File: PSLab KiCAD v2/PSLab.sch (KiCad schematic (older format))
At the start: 73 parts, among them CON1 USB-MINI-B, P10 Analog, P12 5V, P13 MCLR, P2 PROG, P3 DIO, P4 V+/V-, P5 sen-cap, P6 I2C, P7 NRF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

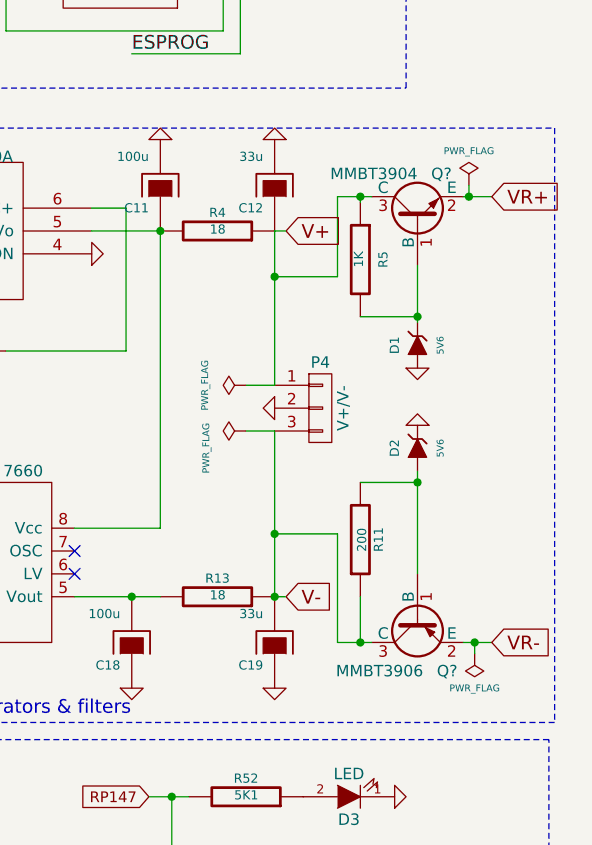
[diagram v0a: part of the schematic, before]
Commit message: Edited R11 value and changed zener voltages
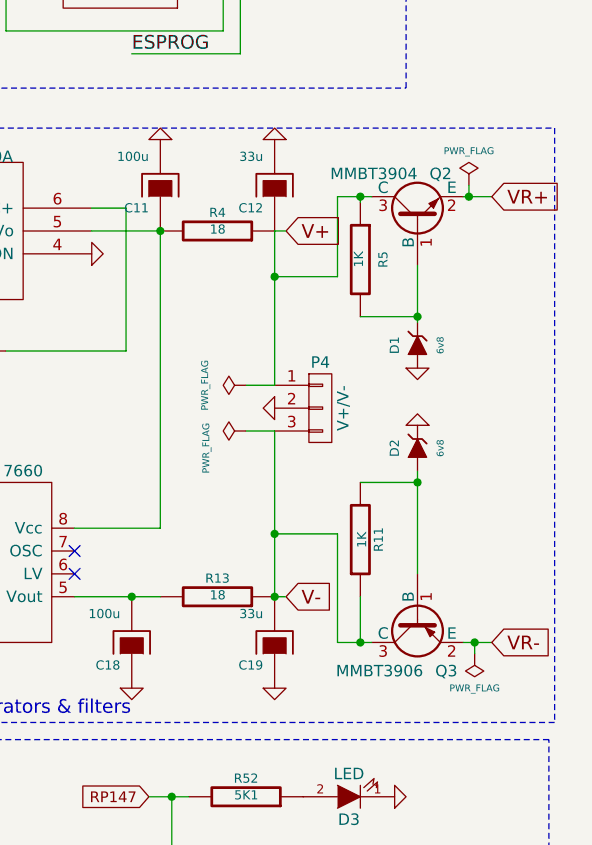
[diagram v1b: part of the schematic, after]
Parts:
- D1, D2: value 5V6 -> 6v8
- R11: value 200 -> 1K
- gave numbers to parts that had none: 2
